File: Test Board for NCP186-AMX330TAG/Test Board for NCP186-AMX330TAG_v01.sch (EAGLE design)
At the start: 7 parts

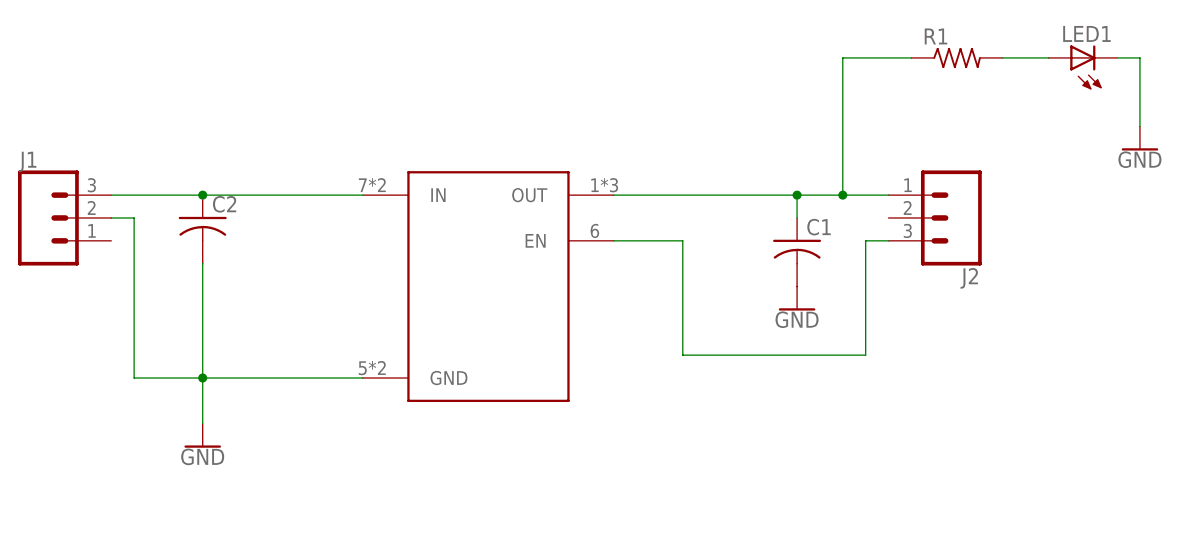
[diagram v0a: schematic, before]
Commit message: Updated NCP part
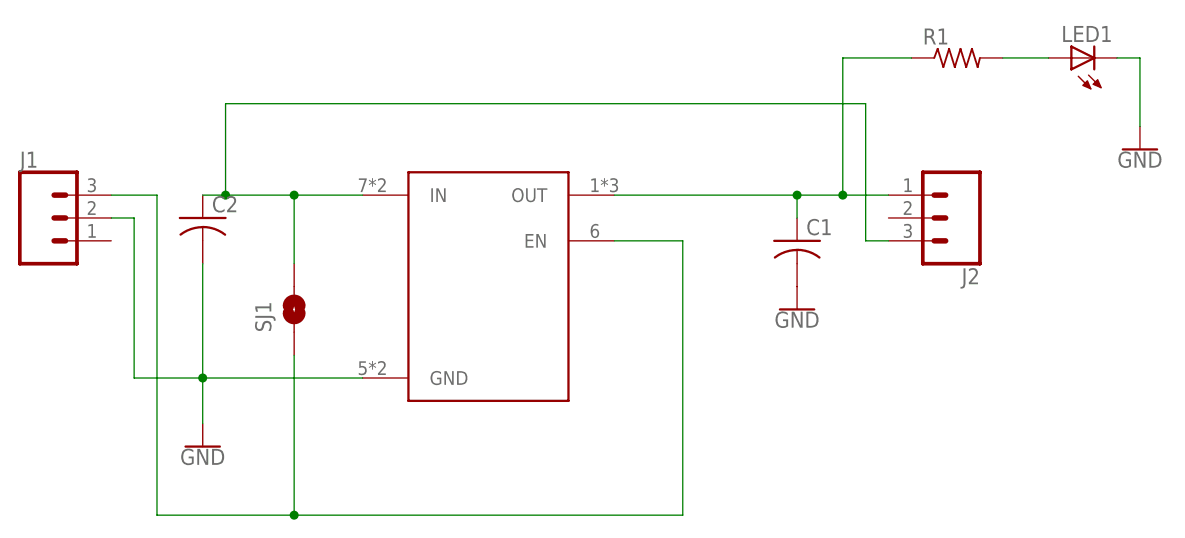
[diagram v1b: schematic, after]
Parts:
- added SJ1: SOLDERJUMPERNO, SparkFun-Retired:SOLDERJUMPERNO
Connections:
- net EN: now also J1.3, SJ1.1; no longer J2.3
- net IIN: now also J2.3, SJ1.2; no longer J1.3
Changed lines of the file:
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@@
 </classes>
 <parts>
-<part name="U$1" library="Ladvien_Eagle_Parts" deviceset="NCP186-AMX330TAG" device=""/>
 <part name="C1" library="resistor" deviceset="C-US" device="C0805K"/>
 <part name="C2" library="resistor" deviceset="C-US" device="C0805K"/>
@@
 <part name="R1" library="resistor" deviceset="R-US_" device="R0805W"/>
 <part name="GND3" library="SparkFun-PowerSymbols" deviceset="GND" device=""/>
+<part name="U$1" library="Ladvien_Eagle_Parts" deviceset="NCP186-AMX330TAG" device=""/>
+<part name="SJ1" library="SparkFun-Retired" deviceset="SOLDERJUMPER" device="NO"/>
 </parts>
 <sheets>
@@
 </plain>
 <instances>
-<instance part="U$1" gate="G$1" x="0" y="25.4"/>
 <instance part="C1" gate="G$1" x="43.18" y="17.78"/>
 <instance part="C2" gate="G$1" x="-22.86" y="20.32"/>
@@
 <instance part="R1" gate="G$1" x="60.96" y="38.1"/>
 <instance part="GND3" gate="1" x="81.28" y="27.94"/>
+<instance part="U$1" gate="G$1" x="0" y="25.4"/>
+<instance part="SJ1" gate="1" x="-12.7" y="10.16" smashed="yes" rot="R90">
+<attribute name="NAME" x="-15.24" y="7.62" size="1.778" layer="95" rot="R90"/>
+</instance>
 </instances>
 <busses>
@@
 <net name="IIN" class="0">
 <segment>
-<pinref part="J1" gate="J$1" pin="3"/>
 <pinref part="C2" gate="G$1" pin="1"/>
-<wire x1="-33.02" y1="22.86" x2="-22.86" y2="22.86" width="0.1524" layer="91"/>
 <pinref part="U$1" gate="G$1" pin="IN"/>
-<wire x1="-22.86" y1="22.86" x2="-5.08" y2="22.86" width="0.1524" layer="91"/>
-<junction x="-22.86" y="22.86"/>
+<wire x1="-20.32" y1="22.86" x2="-12.7" y2="22.86" width="0.1524" layer="91"/>
+<wire x1="-12.7" y1="22.86" x2="-5.08" y2="22.86" width="0.1524" layer="91"/>
+<wire x1="-22.86" y1="22.86" x2="-20.32" y2="22.86" width="0.1524" layer="91"/>
+<wire x1="-20.32" y1="22.86" x2="-20.32" y2="33.02" width="0.1524" layer="91"/>
+<wire x1="-20.32" y1="33.02" x2="50.8" y2="33.02" width="0.1524" layer="91"/>
+<wire x1="50.8" y1="33.02" x2="50.8" y2="17.78" width="0.1524" layer="91"/>
+<pinref part="J2" gate="J$1" pin="3"/>
+<wire x1="50.8" y1="17.78" x2="53.34" y2="17.78" width="0.1524" layer="91"/>
+<junction x="-20.32" y="22.86"/>
+<pinref part="SJ1" gate="1" pin="2"/>
+<wire x1="-12.7" y1="22.86" x2="-12.7" y2="15.24" width="0.1524" layer="91"/>
+<junction x="-12.7" y="22.86"/>
 </segment>
 </net>
@@
 <wire x1="-33.02" y1="20.32" x2="-30.48" y2="20.32" width="0.1524" layer="91"/>
 <wire x1="-30.48" y1="20.32" x2="-30.48" y2="2.54" width="0.1524" layer="91"/>
-<pinref part="U$1" gate="G$1" pin="GND"/>
 <wire x1="-30.48" y1="2.54" x2="-22.86" y2="2.54" width="0.1524" layer="91"/>
 <pinref part="C2" gate="G$1" pin="2"/>
@@
 <pinref part="GND1" gate="1" pin="GND"/>
 <wire x1="-22.86" y1="2.54" x2="-22.86" y2="-2.54" width="0.1524" layer="91"/>
+<pinref part="U$1" gate="G$1" pin="GND"/>
 </segment>
 <segment>
@@
 <net name="OUT" class="0">
 <segment>
-<pinref part="U$1" gate="G$1" pin="OUT"/>
 <wire x1="22.86" y1="22.86" x2="43.18" y2="22.86" width="0.1524" layer="91"/>
 <wire x1="43.18" y1="22.86" x2="48.26" y2="22.86" width="0.1524" layer="91"/>
@@
 <junction x="48.26" y="22.86"/>
 <junction x="43.18" y="22.86"/>
+<pinref part="U$1" gate="G$1" pin="OUT"/>
 </segment>
 </net>
 <net name="EN" class="0">
 <segment>
+<wire x1="22.86" y1="17.78" x2="30.48" y2="17.78" width="0.1524" layer="91"/>
 <pinref part="U$1" gate="G$1" pin="EN"/>
-<wire x1="22.86" y1="17.78" x2="30.48" y2="17.78" width="0.1524" layer="91"/>
-<wire x1="30.48" y1="17.78" x2="30.48" y2="5.08" width="0.1524" layer="91"/>
-<wire x1="30.48" y1="5.08" x2="50.8" y2="5.08" width="0.1524" layer="91"/>
-<wire x1="50.8" y1="5.08" x2="50.8" y2="17.78" width="0.1524" layer="91"/>
-<pinref part="J2" gate="J$1" pin="3"/>
-<wire x1="50.8" y1="17.78" x2="53.34" y2="17.78" width="0.1524" layer="91"/>
+<wire x1="30.48" y1="17.78" x2="30.48" y2="-12.7" width="0.1524" layer="91"/>
+<wire x1="30.48" y1="-12.7" x2="-12.7" y2="-12.7" width="0.1524" layer="91"/>
+<wire x1="-12.7" y1="-12.7" x2="-27.94" y2="-12.7" width="0.1524" layer="91"/>
+<wire x1="-27.94" y1="-12.7" x2="-27.94" y2="22.86" width="0.1524" layer="91"/>
+<pinref part="J1" gate="J$1" pin="3"/>
+<wire x1="-27.94" y1="22.86" x2="-33.02" y2="22.86" width="0.1524" layer="91"/>
+<pinref part="SJ1" gate="1" pin="1"/>
+<wire x1="-12.7" y1="5.08" x2="-12.7" y2="-12.7" width="0.1524" layer="91"/>
+<junction x="-12.7" y="-12.7"/>
 </segment>
 </net>
